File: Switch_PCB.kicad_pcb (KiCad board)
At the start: 2 copper layers, 213 x 96.6 mm, 55 parts, among them J1 Black, J10 Black, J11 Red, J12-0 Conn_01x02, J12-1 Jack 2.1mm, J12-2 Jack 2.1mm, J13 Black, J14 Red, J15 Black, J16 Red, J17 Black, J18 Red, J19 Black, J2 Red, J20 Red, J21 Black, J22 Red, J23 Black, J24 Red, J25 Black, J26 Red, J27 Black, J28 Red, J3 Black, J4 Red, J5 Black, J6 Red, J7 Black, J8 Red, J9 Red, SW1 Switch On-Off-On, SW2 Switch On-Off-On, SW3 Switch On-Off-On, SW4 Switch On-Off-On

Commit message: - Add 3 pin conn for LED states - Start of the routing of the tracks of the electronic card
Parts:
- removed the J18 at (171.9, 100.5)
- removed the J25 at (152.9, 120.8)
- added J13: Conn_01x03, Connector_PinHeader_2.54mm:PinHeader_1x03_P2.54mm_Vertical, F.Cu at (62.7, 87.2)
- added J15: Conn_01x03, Connector_PinHeader_2.54mm:PinHeader_1x03_P2.54mm_Vertical, F.Cu at (159.8, 87.2)
- added J30: Red, ArnauldDev_Connector_Banana:SCHUTZINGER_SWEB8094AU-RT_4mm_Horizontal_Red, F.Cu at (123.4, 120.8)
- added J31: Black, ArnauldDev_Connector_Banana:SCHUTZINGER_SWEB8094AU-SW_4mm_Horizontal_Black, F.Cu at (152.9, 120.8)
- added J32: Red, ArnauldDev_Connector_Banana:SCHUTZINGER_SWEB8094AU-RT_4mm_Horizontal_Red, F.Cu at (171.9, 120.8)
- added J34: Red, ArnauldDev_Connector_Banana:SCHUTZINGER_SWEB8094AU-RT_4mm_Horizontal_Red, F.Cu at (220.4, 120.8)
- J11, J2, J28, J4, J6, J8, J9: footprint ArnauldDev_Connector_Banana:SCHUTZINGER_SWEB8094AU-SW_4mm_Horizontal_Red -> ArnauldDev_Connector_Banana:SCHUTZINGER_SWEB8094AU-RT_4mm_Horizontal_Red
- J14, J16: value Red -> Conn_01x03; footprint ArnauldDev_Connector_Banana:STAUBLI_66.9032-21_XELA-4_4mm_Vertical_Red -> Connector_PinHeader_2.54mm:PinHeader_1x03_P2.54mm_Vertical
- J20: footprint ArnauldDev_Connector_Banana:STAUBLI_66.9032-21_XELA-4_4mm_Vertical_Red -> ArnauldDev_Connector_Banana:STAUBLI_66.9032-22_XELA-4_4mm_Vertical_Red
- J22, J24, J26: footprint ArnauldDev_Connector_Banana:SCHUTZINGER_SWEB8094AU-SW_4mm_Horizontal_Red -> ArnauldDev_Connector_Banana:STAUBLI_66.9032-22_XELA-4_4mm_Vertical_Red
- moved J20 145.5 mm to (74.9, 100.5)
- moved J28 145.5 mm to (74.9, 120.8)
- moved J16 85.9 mm to (208.3, 87.2), turned to 90 degrees
- moved J22 52.6 mm to (123.4, 100.5), turned to 0 degrees
- moved J24 52.6 mm to (171.9, 100.5), turned to 0 degrees
- moved J26 52.6 mm to (220.4, 100.5), turned to 0 degrees
- moved J14 38.8 mm to (111.3, 87.2), turned to 90 degrees
- renumbered J12-0 to J12, J12-1 to J17, J12-2 to J18, J13 to J19, J15 to J21, J17 to J23, J19 to J25, J21 to J27, J23 to J29, J27 to J33
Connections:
- J14 pad 1: RELAY_V1+ -> GNDD
- J16 pad 1: RELAY_V2+ -> GNDD
- J20 pad 1: RELAY_V4+ -> RELAY_V1+
- J22 pad 1: RELAY_V1- -> RELAY_V2+
- J24 pad 1: RELAY_V2- -> RELAY_V3+
- J26 pad 1: RELAY_V3- -> RELAY_V4+
- J28 pad 1: RELAY_V4- -> RELAY_V1-
- R3 pad 2: Net-(R3-Pad2) -> Net-(J14-Pad2)
- R4 pad 2: Net-(R4-Pad2) -> Net-(J14-Pad3)
- R7 pad 2: Net-(R7-Pad2) -> Net-(J16-Pad2)
- R8 pad 2: Net-(R8-Pad2) -> Net-(J16-Pad3)
- SW2 pad 1: Net-(R3-Pad2) -> Net-(J14-Pad2)
- SW2 pad 3: Net-(R4-Pad2) -> Net-(J14-Pad3)
- SW4 pad 1: Net-(R7-Pad2) -> Net-(J16-Pad2)
- SW4 pad 3: Net-(R8-Pad2) -> Net-(J16-Pad3)
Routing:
- net GNDD: track 0.00 -> 196.3 mm
- net Keithley_VA: track 0.00 -> 189.1 mm
- net Keithley_VB: track 0.00 -> 112.9 mm
- net Net-(J15-Pad3): track 0.00 -> 30.5 mm, vias 0 -> 1
- net Net-(J15-Pad2): track 0.00 -> 28.2 mm
- net Alim_V3: track 0.00 -> 25.0 mm
- net Net-(D5-Pad2): track 0.00 -> 4.21 mm
- net Net-(D6-Pad2): track 0.00 -> 3.91 mm
- added copper zone on B.Cu, net GNDPWR
- added copper zone on F.Cu, net GNDPWR
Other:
- net class Connector_Banana: clearance 0.4 -> 0.6
- board text added: "Bottom ground plane"
- board text added: "Top ground plane"

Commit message: Duplicate tracks
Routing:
- net (no net): track 0.00 -> 685.7 mm, vias 0 -> 7
- net +5VD: track 0.00 -> 263.2 mm, vias 0 -> 4
- net RELAY_V1+: track 0.00 -> 66.5 mm, vias 0 -> 1
- net GNDD: track 196.3 -> 259.9 mm
- net RELAY_V4-: track 0.00 -> 36.9 mm
- net RELAY_V1-: track 0.00 -> 36.9 mm
- net RELAY_V3-: track 0.00 -> 36.9 mm
- net Net-(J16-Pad3): track 0.00 -> 34.3 mm, vias 0 -> 1
- net Net-(J13-Pad3): track 0.00 -> 34.3 mm, vias 0 -> 1
- net Net-(J14-Pad3): track 0.00 -> 34.3 mm, vias 0 -> 1
- net Net-(J13-Pad2): track 0.00 -> 28.2 mm
- net Net-(J16-Pad2): track 0.00 -> 28.2 mm
- net Net-(J14-Pad2): track 0.00 -> 28.2 mm
- net Alim_V4: track 0.00 -> 25.0 mm
- net Alim_V2: track 0.00 -> 25.0 mm
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
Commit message: Screen printing validation
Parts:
- moved H1 0.11 mm to (113.8, 61.0)
- moved H2 0.10 mm to (233.8, 60.9)
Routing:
- net (no net): track 685.7 -> 192.4 mm, vias 7 -> 2
- net +5VD: track 263.2 -> 170.0 mm
- net RELAY_V2-: track 0.00 -> 74.2 mm
- net RELAY_V2+: track 0.00 -> 14.8 mm
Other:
- board text added: "+VDC= +5Vdc"
- board text added: "LED ON/OFF"

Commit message: Routing completed
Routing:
- net (no net): track 192.4 -> 0.00 mm, vias 2 -> 0
- net +5VD: track 170.0 -> 265.0 mm, vias 4 -> 1
- net RELAY_V4+: track 0.00 -> 86.6 mm, vias 0 -> 1
- net RELAY_V3+: track 0.00 -> 86.6 mm, vias 0 -> 1
- net RELAY_V2+: track 14.8 -> 86.6 mm, vias 0 -> 1
- net GNDD: track 259.9 -> 326.6 mm
- net +VDC: track 0.00 -> 27.3 mm
- net Keithley_VA: track 190.1 -> 195.1 mm
- net Keithley_VB: track 112.9 -> 114.5 mm

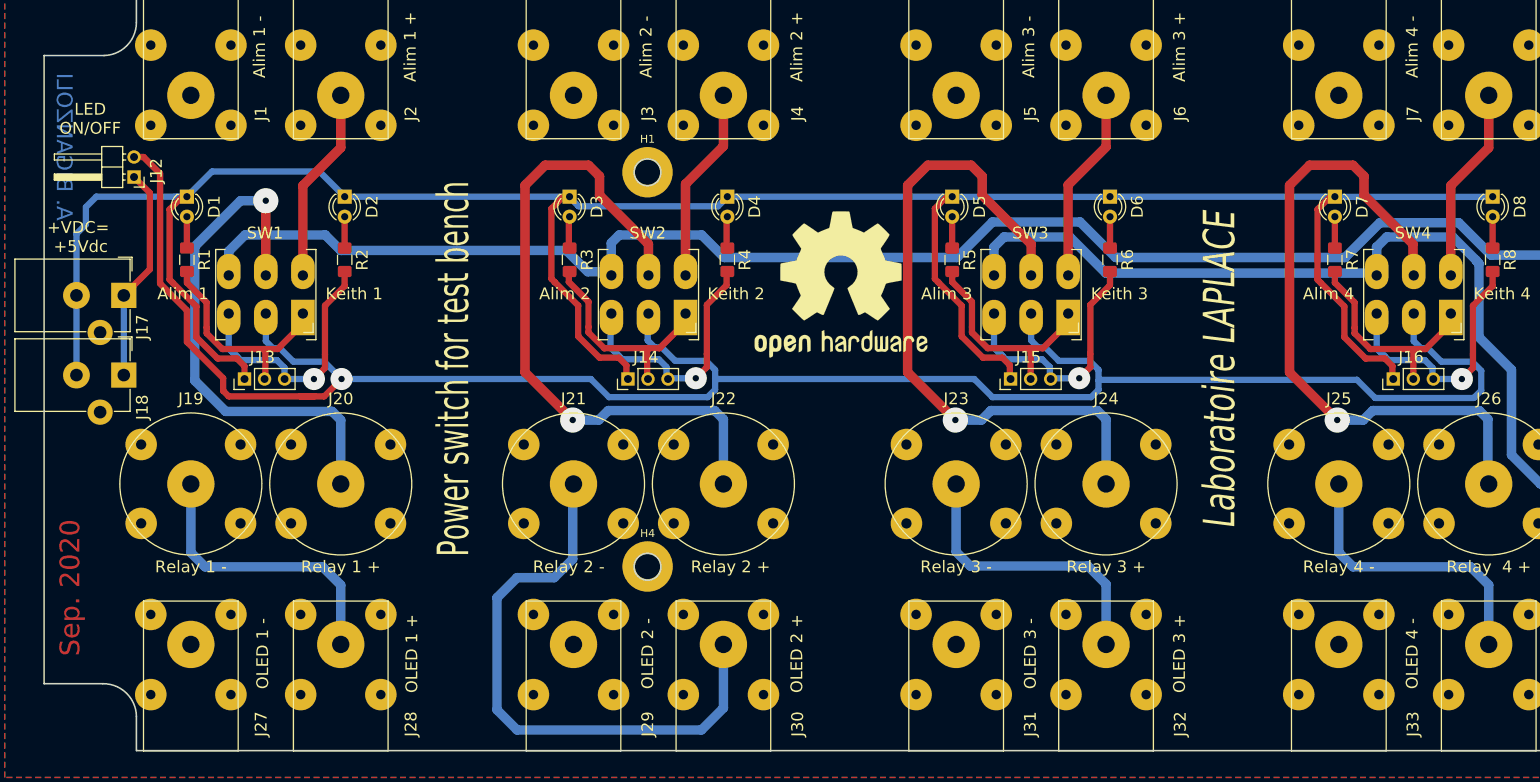
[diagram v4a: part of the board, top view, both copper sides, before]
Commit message: Add via to GNDPWR
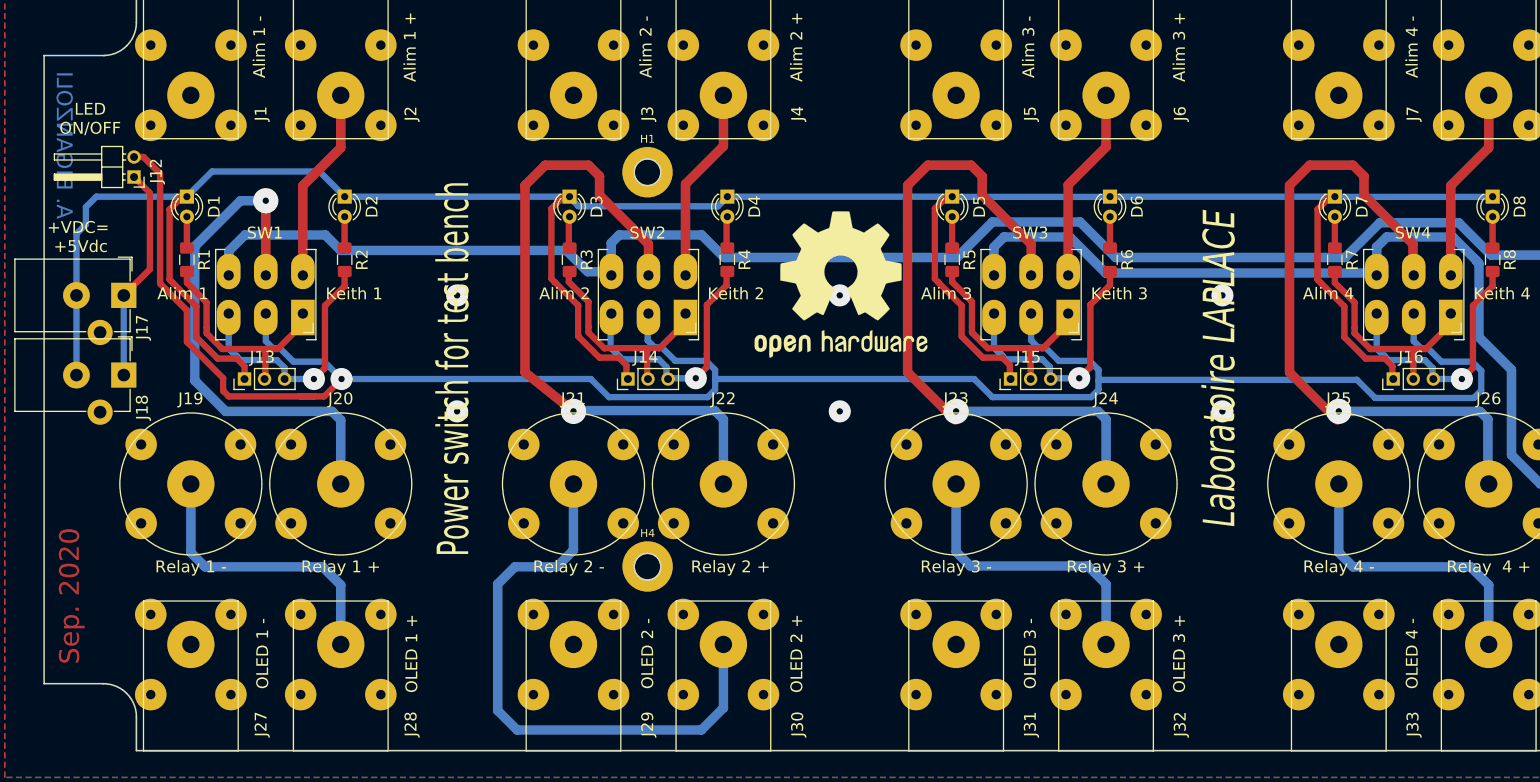
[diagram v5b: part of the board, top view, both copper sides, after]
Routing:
- net RELAY_V2-: track 74.2 -> 75.6 mm
- net RELAY_V2+: track 86.6 -> 85.4 mm
- net RELAY_V4+: track 86.6 -> 85.9 mm
- net RELAY_V3+: track 86.6 -> 86.0 mm
- net GNDPWR: vias 0 -> 6

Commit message: Project review and mechanical integration
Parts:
- added ?: KiCad-Logo2_5mm_SilkScreen, Symbol:KiCad-Logo2_5mm_SilkScreen, F.Cu at (138.3, 60.5)
